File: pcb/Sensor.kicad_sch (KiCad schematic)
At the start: 60 parts, among them IC2 74HC14D-Q100,118, U2 OPA2376xxD, U5 OPA2376xxD

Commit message: fixed LEDs footprints
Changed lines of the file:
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@@
 	(global_label "SPARK_TRIGGER"
 		(shape input)
-		(at 182.88 143.51 270)
+		(at 182.88 143.51 180)
 		(fields_autoplaced yes)
 		(effects
@@
 		)
 		(property "Intersheetrefs" "${INTERSHEET_REFS}"
-			(at 182.88 161.3723 90)
+			(at 165.0177 143.51 0)
 			(effects
 				(font

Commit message: fixed pcb import errors
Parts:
- renumbered U5 to U2
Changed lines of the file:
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@@
 		(dnp no)
 		(fields_autoplaced yes)
-		(property "Reference" "U5"
+		(property "Reference" "U2"
 			(at 130.81 119.38 0)
 			(effects
@@
 			(project "ecu-dev-board"
 				(path "/38d4df77-b5a0-4642-8410-8b13c21c2c3b/4580a192-f0d7-44eb-b345-2965a93c3023"
-					(reference "U5")
+					(reference "U2")
 					(unit 2)
 				)

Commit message: added custom footprint for external relay
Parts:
- R22: value 270k -> 220k
- renumbered U5 to U2
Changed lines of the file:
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@@
 			)
 		)
-		(property "Value" "270k"
+		(property "Value" "220k"
 			(at 224.79 37.084 0)
 			(effects
@@
 		(dnp no)
 		(fields_autoplaced yes)
-		(property "Reference" "U5"
+		(property "Reference" "U2"
 			(at 116.84 181.6099 0)
 			(effects
@@
 			(project ""
 				(path "/38d4df77-b5a0-4642-8410-8b13c21c2c3b/4580a192-f0d7-44eb-b345-2965a93c3023"
-					(reference "U5")
+					(reference "U2")
 					(unit 3)
 				)

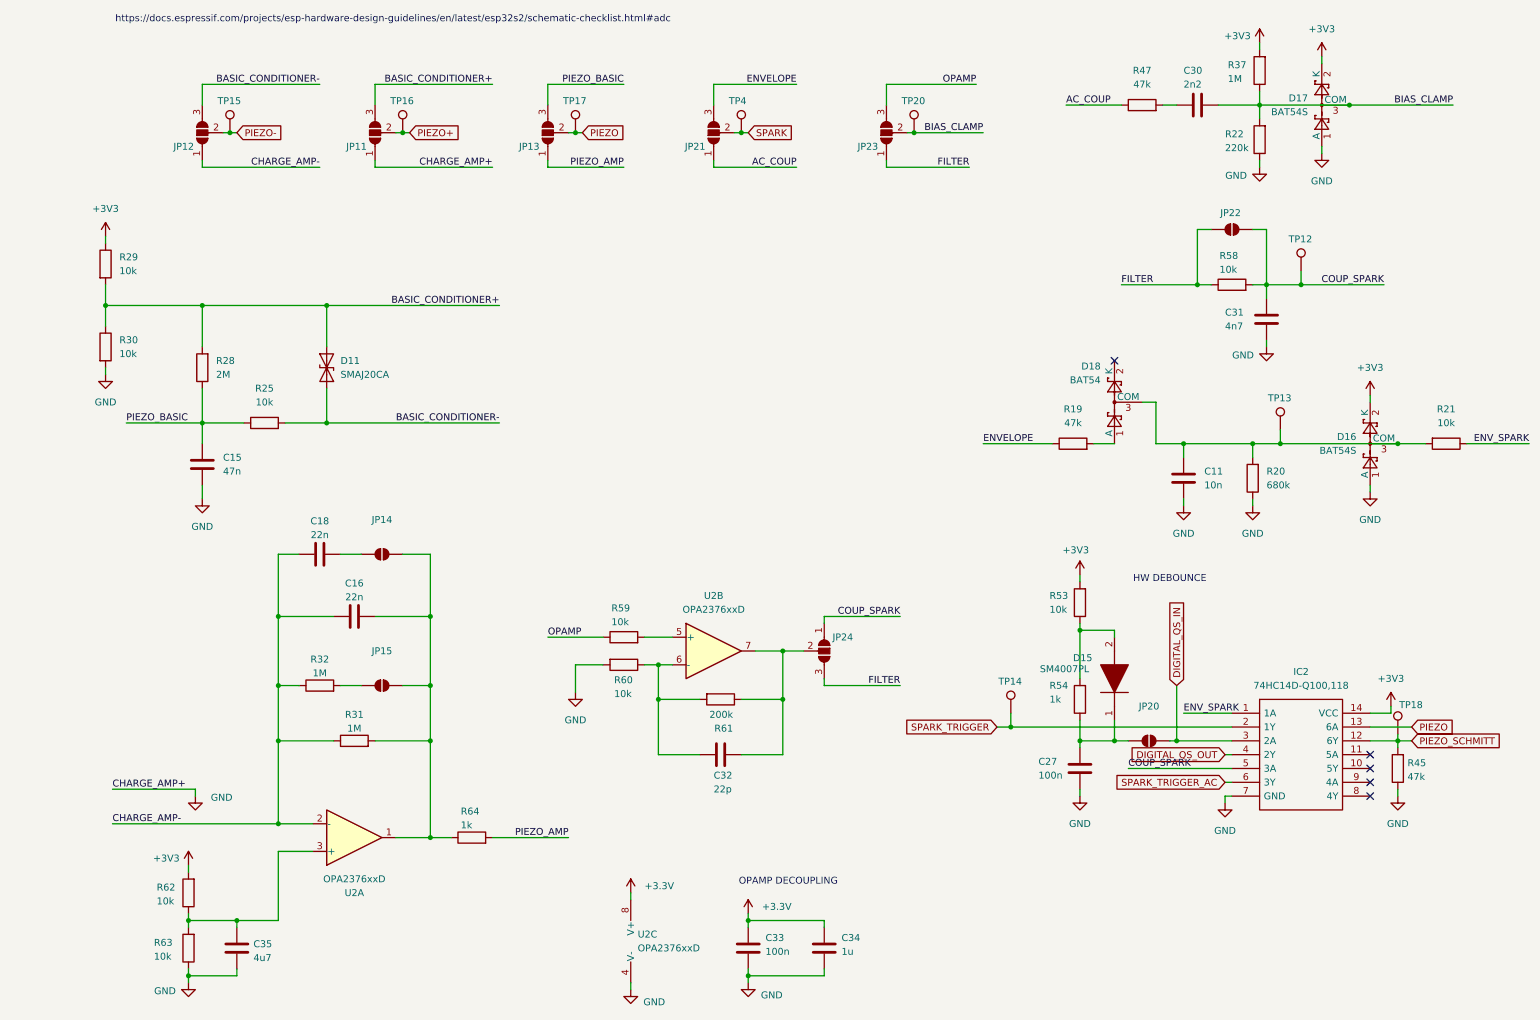
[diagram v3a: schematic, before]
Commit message: added DNP for fabrication and 2P molex connector, minor fixes
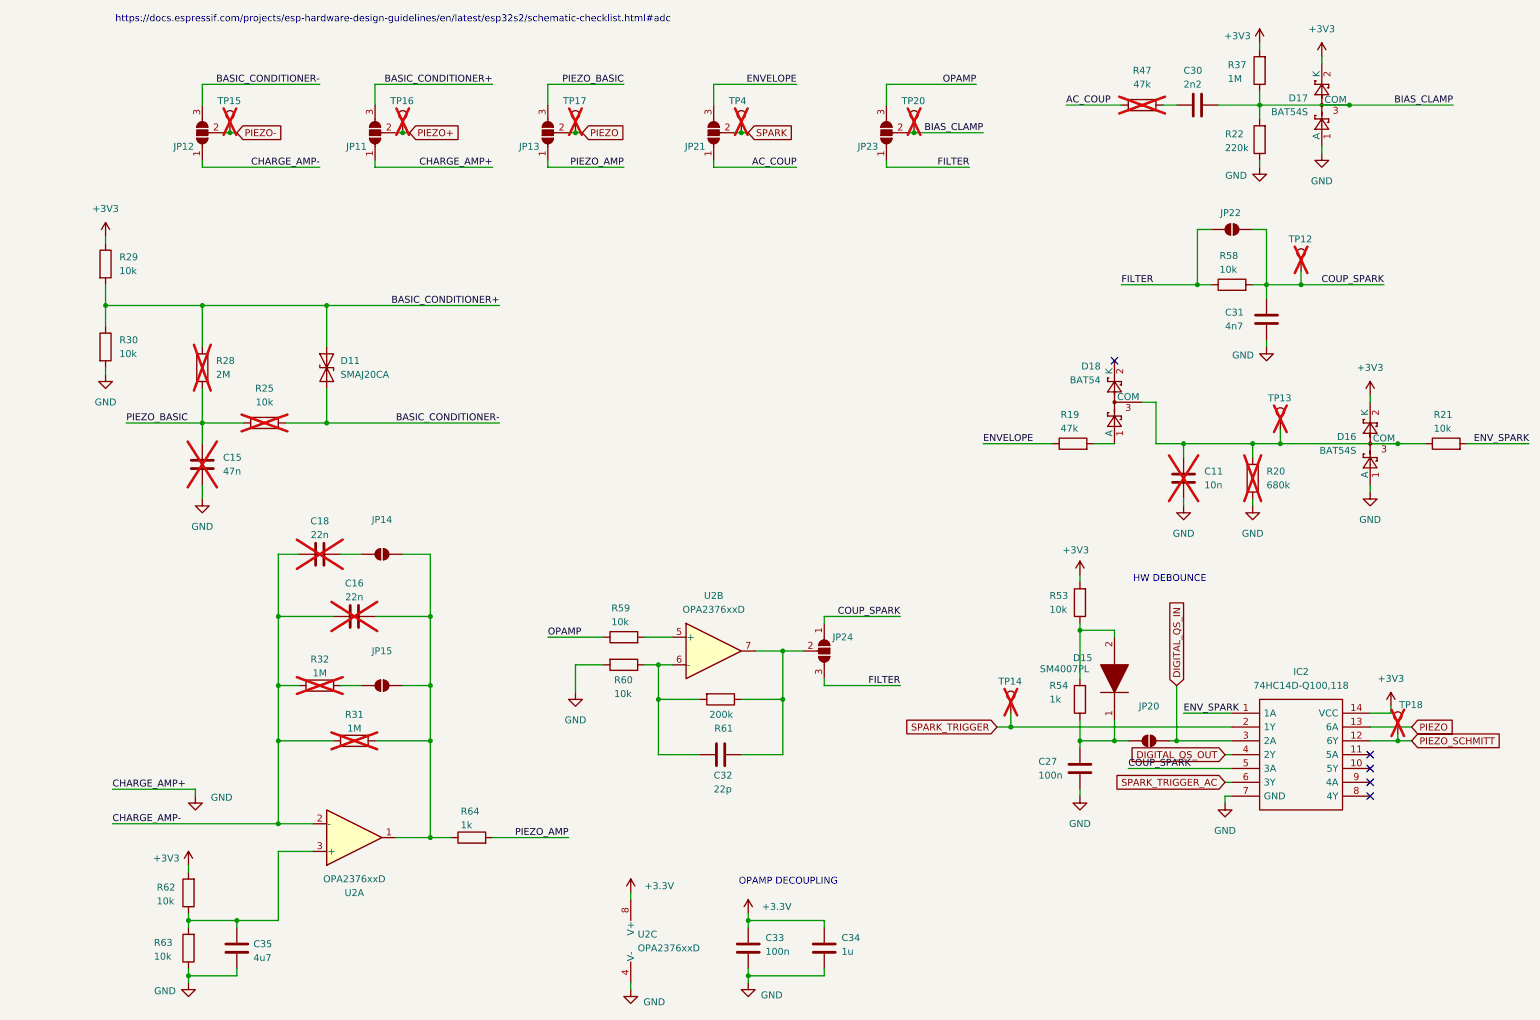
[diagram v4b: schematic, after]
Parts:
- removed R45: 47k, Resistor_SMD:R_0603_1608Metric, symbol Device:R
- C11, C15, C16, C18, R20, R25, R28, R31, R32, R47: now not fitted
- R19, R21: footprint Resistor_THT:R_Axial_DIN0204_L3.6mm_D1.6mm_P1.90mm_Vertical -> Resistor_SMD:R_0603_1608Metric
- TP12, TP13, TP14, TP15, TP16, TP17, TP18, TP20, TP4: footprint Connector_PinHeader_1.00mm:PinHeader_1x01_P1.00mm_Vertical -> Connector_PinHeader_2.54mm:PinHeader_1x01_P2.54mm_Vertical; now not fitted
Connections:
- net ENV_SPARK: now also R21.2; no longer R21.1
- net at C11.1, D16.3 (COM), D18.3 (COM)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: now also R21.1; no longer R21.2

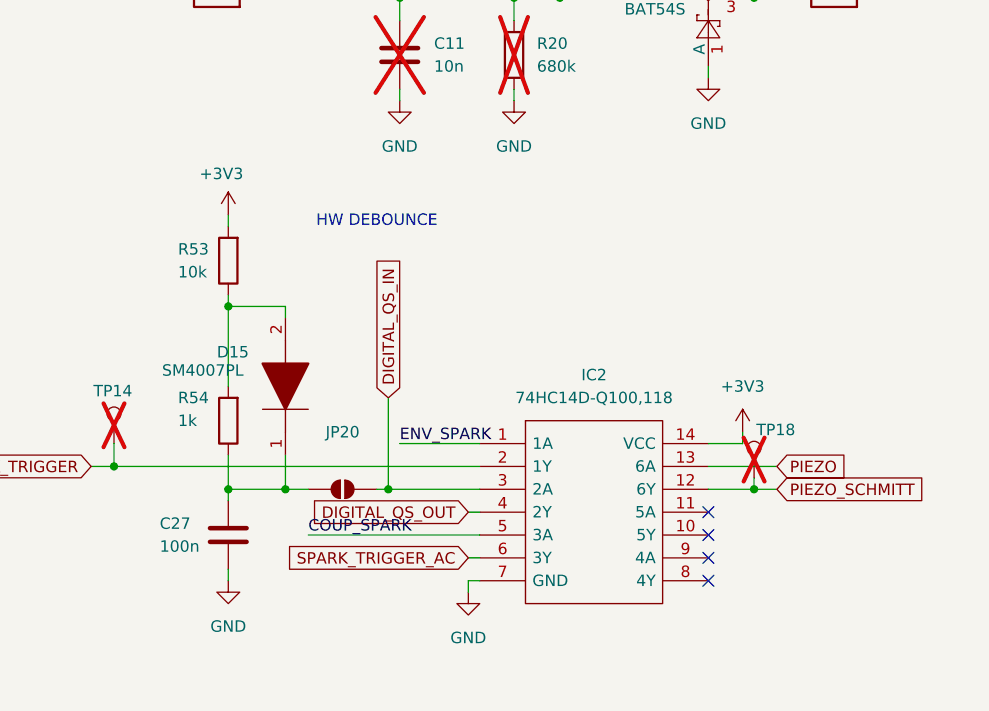
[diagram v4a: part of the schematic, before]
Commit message: added another CDI output sensing (opto coupler)
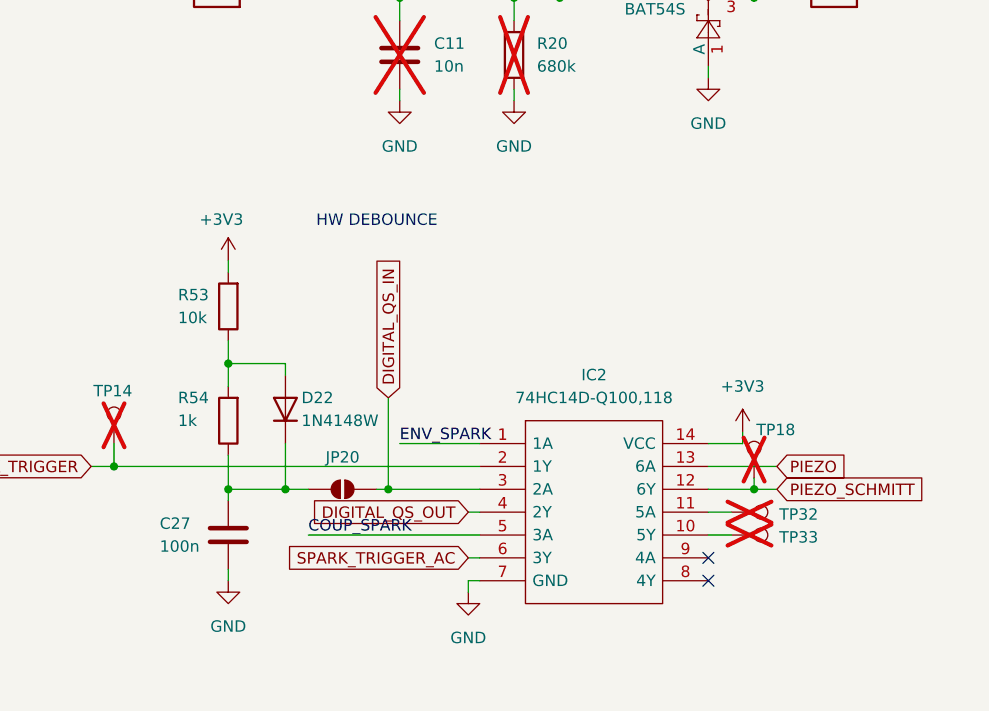
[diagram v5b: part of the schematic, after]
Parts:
- removed D15: SM4007PL, SamacSys_Parts:SODFL3718X125N, symbol SamacSys_Parts:SM4007PL
- added D22: 1N4148W, Diode_SMD:D_SOD-123, symbol Diode:1N4148W
- added TP32, TP33: TestPoint, Connector_PinHeader_2.54mm:PinHeader_1x01_P2.54mm_Vertical, symbol Connector:TestPoint
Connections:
- net at C27.2, JP20.2 (B), R54.1: now also D22.1 (K)
- net at R53.1, R54.2: now also D22.2 (A)
- net at IC2.10 (5Y): now also TP33.1
- net at IC2.11 (5A): now also TP32.1
- no-connect marks 5 -> 3
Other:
- moved on the sheet: R53

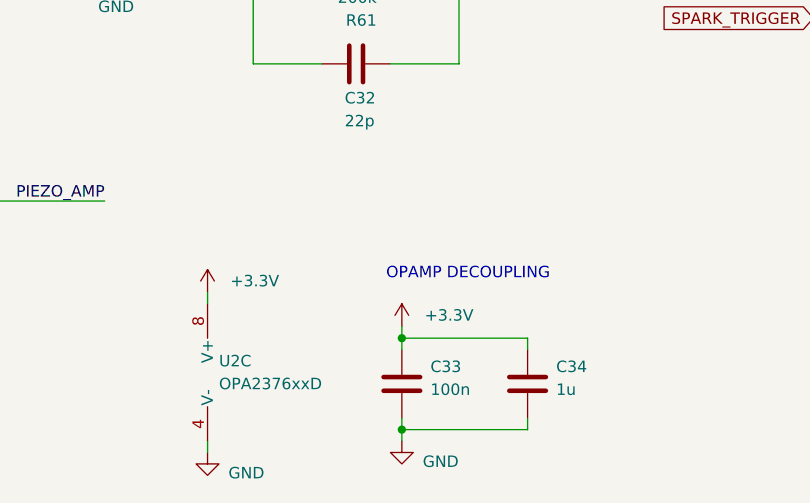
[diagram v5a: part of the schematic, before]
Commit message: fixed 3.3 and 3V3
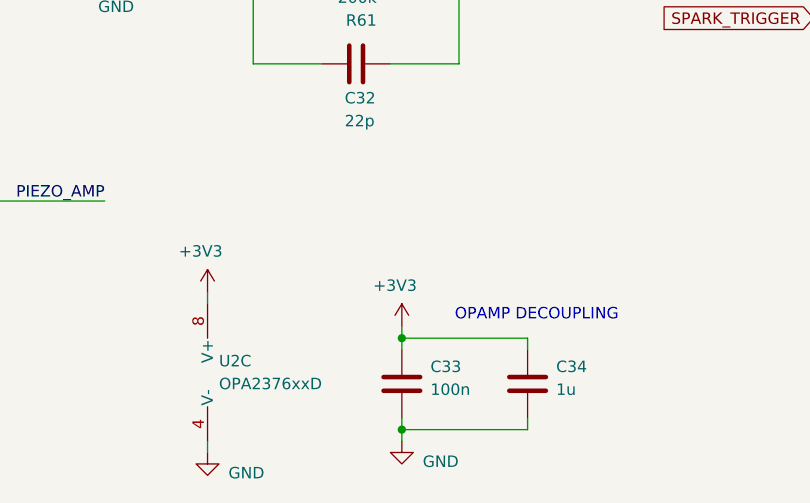
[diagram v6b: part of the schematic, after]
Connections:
- net +3.3V is gone; now on net +3V3: C33.1, C34.1, U2.8 (V+)
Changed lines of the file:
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@@
 	(text "OPAMP DECOUPLING\n"
 		(exclude_from_sim no)
-		(at 144.526 171.958 0)
+		(at 152.146 176.53 0)
 		(effects
 			(font
@@
 	)
 	(symbol
+		(lib_id "power:+3V3")
+		(at 115.57 173.99 0)
+		(unit 1)
+		(exclude_from_sim no)
+		(in_bom yes)
+		(on_board yes)
+		(dnp no)
+		(property "Reference" "#PWR023"
+			(at 115.57 177.8 0)
+			(effects
+				(font
+					(size 1.27 1.27)
+				)
+				(hide yes)
+			)
+		)
+		(property "Value" "+3V3"
+			(at 114.808 169.418 0)
+			(effects
+				(font
+					(size 1.27 1.27)
+				)
+			)
+		)
+		(property "Footprint" ""
+			(at 115.57 173.99 0)
+			(effects
+				(font
+					(size 1.27 1.27)
+				)
+				(hide yes)
+			)
+		)
+		(property "Datasheet" ""
+			(at 115.57 173.99 0)
+			(effects
+				(font
+					(size 1.27 1.27)
+				)
+				(hide yes)
+			)
+		)
+		(property "Description" "Power symbol creates a global label with name \"+3V3\""
+			(at 115.57 173.99 0)
+			(effects
+				(font
+					(size 1.27 1.27)
+				)
+				(hide yes)
+			)
+		)
+		(pin "1"
+		)
+		(instances
+			(project "ecu-dev-board"
+				(path "/38d4df77-b5a0-4642-8410-8b13c21c2c3b/4580a192-f0d7-44eb-b345-2965a93c3023"
+					(reference "#PWR023")
+					(unit 1)
+				)
+			)
+		)
+	)
+	(symbol
 		(lib_id "Device:C")
 		(at 217.17 97.79 0)
@@
 	)
 	(symbol
-		(lib_id "power:+3.3V")
-		(at 115.57 173.99 0)
-		(unit 1)
-		(exclude_from_sim no)
-		(in_bom yes)
-		(on_board yes)
-		(dnp no)
-		(fields_autoplaced yes)
-		(property "Reference" "#PWR031"
-			(at 115.57 177.8 0)
-			(effects
-				(font
-					(size 1.27 1.27)
-				)
-				(hide yes)
-			)
-		)
-		(property "Value" "+3.3V"
-			(at 118.11 172.7199 0)
-			(effects
-				(font
-					(size 1.27 1.27)
-				)
-				(justify left)
-			)
-		)
-		(property "Footprint" ""
-			(at 115.57 173.99 0)
-			(effects
-				(font
-					(size 1.27 1.27)
-				)
-				(hide yes)
-			)
-		)
-		(property "Datasheet" ""
-			(at 115.57 173.99 0)
-			(effects
-				(font
-					(size 1.27 1.27)
-				)
-				(hide yes)
-			)
-		)
-		(property "Description" "Power symbol creates a global label with name \"+3.3V\""
-			(at 115.57 173.99 0)
-			(effects
-				(font
-					(size 1.27 1.27)
-				)
-				(hide yes)
-			)
-		)
-		(pin "1"
-		)
-		(instances
-			(project "ecu-dev-board"
-				(path "/38d4df77-b5a0-4642-8410-8b13c21c2c3b/4580a192-f0d7-44eb-b345-2965a93c3023"
-					(reference "#PWR031")
-					(unit 1)
-				)
-			)
-		)
-	)
-	(symbol
 		(lib_id "Jumper:SolderJumper_3_Open")
 		(at 130.81 34.29 90)
@@
 	)
 	(symbol
-		(lib_id "power:+3.3V")
-		(at 137.16 177.8 0)
-		(unit 1)
-		(exclude_from_sim no)
-		(in_bom yes)
-		(on_board yes)
-		(dnp no)
-		(fields_autoplaced yes)
-		(property "Reference" "#PWR078"
-			(at 137.16 181.61 0)
-			(effects
-				(font
-					(size 1.27 1.27)
-				)
-				(hide yes)
-			)
-		)
-		(property "Value" "+3.3V"
-			(at 139.7 176.5299 0)
-			(effects
-				(font
-					(size 1.27 1.27)
-				)
-				(justify left)
-			)
-		)
-		(property "Footprint" ""
-			(at 137.16 177.8 0)
-			(effects
-				(font
-					(size 1.27 1.27)
-				)
-				(hide yes)
-			)
-		)
-		(property "Datasheet" ""
-			(at 137.16 177.8 0)
-			(effects
-				(font
-					(size 1.27 1.27)
-				)
-				(hide yes)
-			)
-		)
-		(property "Description" "Power symbol creates a global label with name \"+3.3V\""
-			(at 137.16 177.8 0)
-			(effects
-				(font
-					(size 1.27 1.27)
-				)
-				(hide yes)
-			)
-		)
-		(pin "1"
-		)
-		(instances
-			(project "ecu-dev-board"
-				(path "/38d4df77-b5a0-4642-8410-8b13c21c2c3b/4580a192-f0d7-44eb-b345-2965a93c3023"
-					(reference "#PWR078")
-					(unit 1)
-				)
-			)
-		)
-	)
-	(symbol
 		(lib_id "Device:R")
 		(at 64.77 146.05 90)
@@
 					(unit 1)
 				)
+			)
+		)
+	)
+	(symbol
+		(lib_id "power:+3V3")
+		(at 137.16 177.8 0)
+		(unit 1)
+		(exclude_from_sim no)
+		(in_bom yes)
+		(on_board yes)
+		(dnp no)
+		(property "Reference" "#PWR022"
+			(at 137.16 181.61 0)
+			(effects
+				(font
+					(size 1.27 1.27)
+				)
+				(hide yes)
+			)
+		)
+		(property "Value" "+3V3"
+			(at 136.398 173.228 0)
+			(effects
+				(font
+					(size 1.27 1.27)
+				)
+			)
+		)
+		(property "Footprint" ""
+			(at 137.16 177.8 0)
+			(effects
+				(font
+					(size 1.27 1.27)
+				)
+				(hide yes)
+			)
+		)
+		(property "Datasheet" ""
+			(at 137.16 177.8 0)
+			(effects
+				(font
+					(size 1.27 1.27)
+				)
+				(hide yes)
+			)
+		)
+		(property "Description" "Power symbol creates a global label with name \"+3V3\""
+			(at 137.16 177.8 0)
+			(effects
+				(font
+					(size 1.27 1.27)
+				)
+				(hide yes)
+			)
+		)
+		(pin "1"
+		)
+		(instances
+			(project "ecu-dev-board"
+				(path "/38d4df77-b5a0-4642-8410-8b13c21c2c3b/4580a192-f0d7-44eb-b345-2965a93c3023"
+					(reference "#PWR022")
+					(unit 1)
+				)
